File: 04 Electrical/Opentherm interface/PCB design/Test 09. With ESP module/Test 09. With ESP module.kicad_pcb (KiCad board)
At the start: 2 copper layers, 72 x 32 mm, 31 parts, among them J1 OpenTherm, J2 Laser range sensor, J3 ST7789, J4 Encoder, J6 USB_C_Receptacle_USB2.0_16P, Q1 MMBT2907A, U1 DS18S20, U2 DS18S20, U3 DS18S20, U4 DS18S20, U5 EL357N-G, U6 EL357N-G, U7 mini_esp32, U8 ESP32-S3-WROOM-1

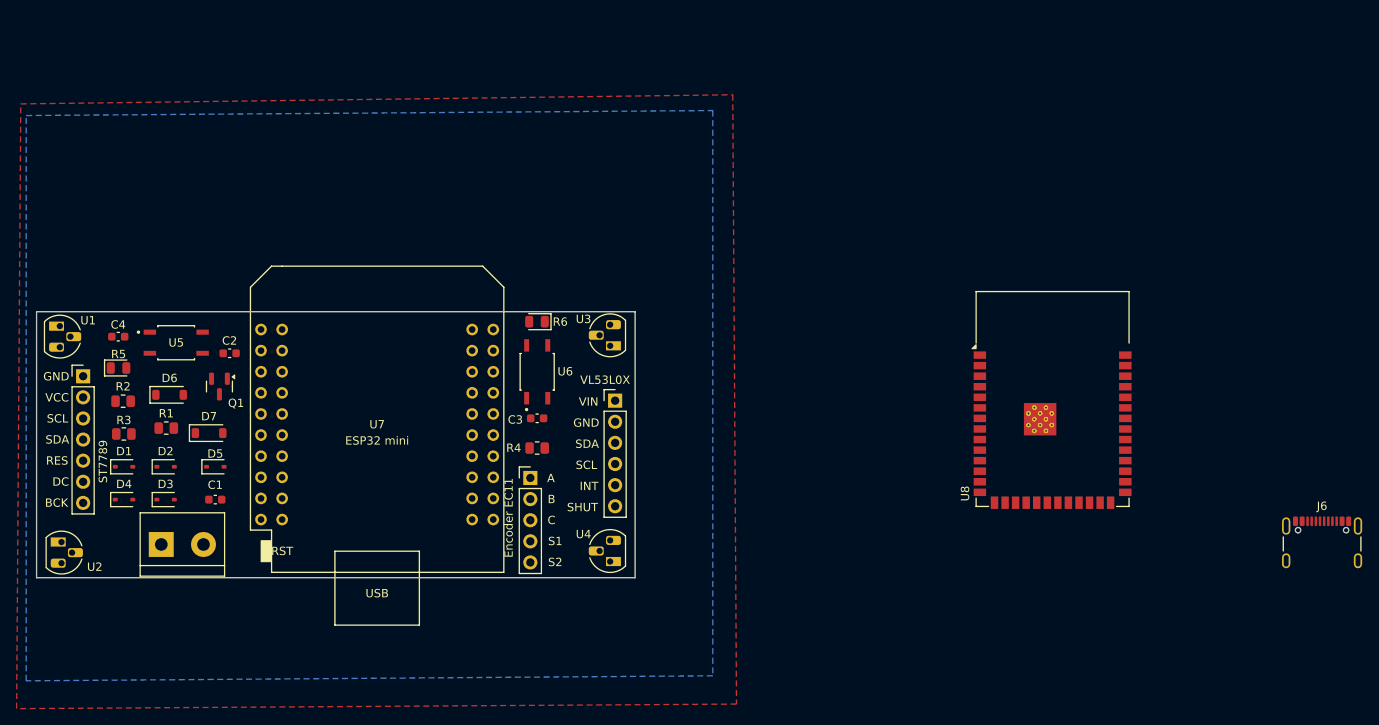
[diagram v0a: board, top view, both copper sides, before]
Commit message: First version of PCB without errors
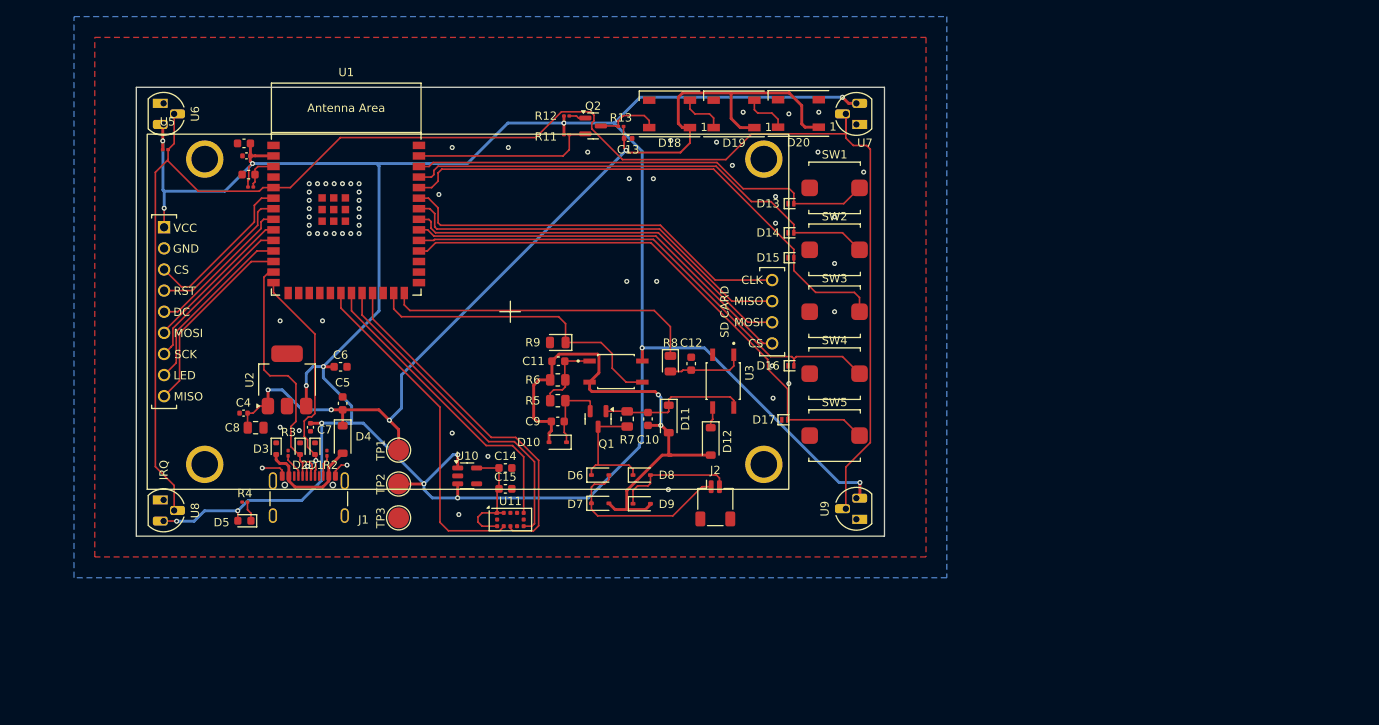
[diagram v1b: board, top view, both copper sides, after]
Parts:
- removed J3: ST7789, Connector_PinHeader_2.54mm:PinHeader_1x07_P2.54mm_Vertical
- removed J4: Encoder, Connector_PinHeader_2.54mm:PinHeader_1x05_P2.54mm_Vertical
- removed J6: USB_C_Receptacle_USB2.0_16P, Connector_USB:USB_C_Receptacle_GCT_USB4105-xx-A_16P_TopMnt_Horizontal
- added C10: 2n2, Capacitor_SMD:C_0603_1608Metric, F.Cu at (166.6, 87.9)
- added C11: 10n, Capacitor_SMD:C_0603_1608Metric, F.Cu at (155.8, 81.0)
- added C12: 2n2, Capacitor_SMD:C_0603_1608Metric, F.Cu at (171.8, 81.2)
- added C13: 10u, Capacitor_SMD:C_0402_1005Metric, F.Cu at (164.2, 54.1)
- added C14: 0.1u, Capacitor_SMD:C_0603_1608Metric, F.Cu at (149.4, 93.8)
- added C15: 4.7pF, Capacitor_SMD:C_0603_1608Metric, F.Cu at (149.4, 96.3)
- added C5: 0.1u, Capacitor_SMD:C_0603_1608Metric, F.Cu at (129.8, 86.0)
- added C6: 0.1u, Capacitor_SMD:C_0603_1608Metric, F.Cu at (129.6, 81.6)
- added C7: 10u, Capacitor_SMD:C_0402_1005Metric, F.Cu at (126.0, 88.9)
- added C8: 22u, Capacitor_SMD:C_0805_2012Metric, F.Cu at (119.3, 89.0)
- added C9: 10n, Capacitor_SMD:C_0603_1608Metric, F.Cu at (155.7, 88.2)
- added D10: BZT52C4V7S, Diode_SMD:D_SOD-323, F.Cu at (155.7, 90.7)
- added D11: BZT52C15V, Diode_SMD:D_SOD-123, F.Cu at (169.1, 87.9)
- added D12: BZT52C4V3, Diode_SMD:D_SOD-123, F.Cu at (174.1, 90.6)
- added D13: LESD8D3.3CAT5G-ES, Diode_SMD:D_SOD-882, F.Cu at (183.8, 62.0)
- added D14: LESD8D3.3CAT5G-ES, Diode_SMD:D_SOD-882, F.Cu at (183.8, 65.5)
- added D15: LESD8D3.3CAT5G-ES, Diode_SMD:D_SOD-882, F.Cu at (183.8, 68.5)
- added D16: LESD8D3.3CAT5G-ES, Diode_SMD:D_SOD-882, F.Cu at (183.8, 81.5)
- added D17: LESD8D3.3CAT5G-ES, Diode_SMD:D_SOD-882, F.Cu at (183.0, 88.0)
- added D18: WS2812B-2020, LED_SMD:LED_WS2812B_PLCC4_5.0x5.0mm_P3.2mm, F.Cu at (169.2, 51.2)
- added D19: WS2812B-2020, LED_SMD:LED_WS2812B_PLCC4_5.0x5.0mm_P3.2mm, F.Cu at (176.9, 51.2)
- added D20: WS2812B-2020, LED_SMD:LED_WS2812B_PLCC4_5.0x5.0mm_P3.2mm, F.Cu at (184.7, 51.1)
- added D8: 1N4148WS, Diode_SMD:D_SOD-323, F.Cu at (165.8, 94.7)
- added D9: 1N4148WS, Diode_SMD:D_SOD-323, F.Cu at (165.8, 98.1)
- added Q2: LBSS138LT1G-ES, Package_TO_SOT_SMD:SOT-23, F.Cu at (159.9, 52.6)
- added R10: 4k7, Resistor_SMD:R_0201_0603Metric, F.Cu at (108.5, 55.5)
- added R11: 10k, Resistor_SMD:R_0201_0603Metric, F.Cu at (156.8, 53.7)
- added R12: 10k, Resistor_SMD:R_0201_0603Metric, F.Cu at (156.8, 51.5)
- added R13: 10k, Resistor_SMD:R_0201_0603Metric, F.Cu at (163.3, 52.7)
- added R7: 330, Resistor_SMD:R_0805_2012Metric, F.Cu at (164.1, 87.9)
- added R8: 1k5, Diode_SMD:D_0805_2012Metric, F.Cu at (169.2, 81.2)
- added R9: 330, Diode_SMD:D_0805_2012Metric, F.Cu at (155.7, 78.7)
- added SW1: btn_home, Project:SW_Push_SPEH, F.Cu at (189.0, 60.1)
- added SW2: btn_up, Project:SW_Push_SPEH, F.Cu at (189.0, 67.5)
- added SW3: btn_down, Project:SW_Push_SPEH, F.Cu at (189.0, 75.0)
- added SW4: btn_confirm, Project:SW_Push_SPEH, F.Cu at (189.0, 82.5)
- added SW5: btn_back, Project:SW_Push_SPEH, F.Cu at (189.0, 89.9)
- added TP1: 5V, TestPoint:TestPoint_Pad_D2.5mm, F.Cu at (136.6, 91.7)
- added TP2: 3V3, TestPoint:TestPoint_Pad_D2.5mm, F.Cu at (136.6, 95.7)
- added TP3: GND, TestPoint:TestPoint_Pad_D2.5mm, F.Cu at (136.6, 99.8)
- added U10: LP5907MFX-2.8/NOPB, Package_TO_SOT_SMD:SOT-23-5, F.Cu at (144.8, 94.8)
- added U11: VL53L0CXV0DH/1, Sensor_Distance:ST_VL53L1x, F.Cu at (150.0, 100.0)
- added U9: DS18S20, Package_TO_SOT_THT:TO-92L_HandSolder, F.Cu at (191.6, 100.0)
- C1: value 10n -> 1u
- C2: value 2n2 -> 0.1u
- C3: value 10n -> 10u; footprint Capacitor_SMD:C_0603_1608Metric -> Capacitor_SMD:C_0402_1005Metric
- C4: value 2n2 -> 10u; footprint Capacitor_SMD:C_0603_1608Metric -> Capacitor_SMD:C_0402_1005Metric
- D1, D2, D3: value 1N4148WS -> LESD5D5.0CT1G; footprint Diode_SMD:D_SOD-323 -> Diode_SMD:D_SOD-523
- D4: value 1N4148WS -> 1N5819HW-7-F; footprint Diode_SMD:D_SOD-323 -> Diode_SMD:D_SOD-123
- D5: value BZT52C4V7S -> C2286; footprint Diode_SMD:D_SOD-323 -> LED_SMD:LED_0603_1608Metric
- D6: value BZT52C15V -> 1N4148WS; footprint Diode_SMD:D_SOD-123 -> Diode_SMD:D_SOD-323
- D7: value BZT52C4V3 -> 1N4148WS; footprint Diode_SMD:D_SOD-123 -> Diode_SMD:D_SOD-323
- J1: value OpenTherm -> USB-C port; footprint TerminalBlock:TerminalBlock_bornier-2_P5.08mm -> Connector_USB:USB_C_Receptacle_GCT_USB4105-xx-A_16P_TopMnt_Horizontal
- J2: value Laser range sensor -> Boiler; footprint Connector_PinHeader_2.54mm:PinHeader_1x06_P2.54mm_Vertical -> Connector_JST:JST_SH_SM02B-SRSS-TB_1x02-1MP_P1.00mm_Horizontal
- R1: value 200 -> 10k; footprint Resistor_SMD:R_0805_2012Metric -> Resistor_SMD:R_0201_0603Metric
- R2: value 150 -> 4k7; footprint Resistor_SMD:R_0805_2012Metric -> Resistor_SMD:R_0201_0603Metric
- R3: value 330 -> 4k7; footprint Resistor_SMD:R_0805_2012Metric -> Resistor_SMD:R_0201_0603Metric
- R4: value 4k7 -> 5k1; footprint Resistor_SMD:R_0805_2012Metric -> Resistor_SMD:R_0201_0603Metric
- R5: value 1k5 -> 200; footprint Diode_SMD:D_0805_2012Metric -> Resistor_SMD:R_0805_2012Metric
- R6: value 330 -> 150; footprint Diode_SMD:D_0805_2012Metric -> Resistor_SMD:R_0805_2012Metric
- U1: value DS18S20 -> ESP32-S3-WROOM-1-N8R2; footprint Package_TO_SOT_THT:TO-92L_HandSolder -> PCM_Espressif:ESP32-S3-WROOM-1
- U2: value DS18S20 -> SGM2212-3.3XKC3G/TR; footprint Package_TO_SOT_THT:TO-92L_HandSolder -> Package_TO_SOT_SMD:SOT-223-3_TabPin2
- U3, U4: value DS18S20 -> EL357N-G; footprint Package_TO_SOT_THT:TO-92L_HandSolder -> EL357N-G:OPTO_EL357N-G
- U5: value EL357N-G -> ILI9341_no_touch; footprint EL357N-G:OPTO_EL357N-G -> Project:ILI9341_no_touch
- U6: value EL357N-G -> DS18S20; footprint EL357N-G:OPTO_EL357N-G -> Package_TO_SOT_THT:TO-92L_HandSolder
- U7: value mini_esp32 -> DS18S20; footprint ESP32_mini:ESP32_mini -> Package_TO_SOT_THT:TO-92L_HandSolder
- U8: value ESP32-S3-WROOM-1 -> DS18S20; footprint RF_Module:ESP32-S3-WROOM-1 -> Package_TO_SOT_THT:TO-92L_HandSolder
- moved U8 107.6 mm to (108.3, 97.6), turned to -90 degrees
- moved U7 68.0 mm to (191.6, 52.5), turned to 90 degrees
- moved U6 55.3 mm to (108.3, 49.9), turned to -90 degrees
- moved R5 53.0 mm to (155.7, 85.7), turned to 180 degrees
- moved D6 52.7 mm to (160.8, 94.7)
- moved D7 47.8 mm to (160.8, 98.0)
- moved C3 47.1 mm to (118.2, 56.2)
- moved Q1 45.7 mm to (160.6, 87.9)
- moved U5 40.4 mm to (150.0, 75.0)
- moved C1 39.3 mm to (118.5, 58.5)
- moved U1 37.0 mm to (130.2, 63.2), turned to 0 degrees
- moved R4 35.8 mm to (118.0, 97.9)
- moved U2 33.4 mm to (123.1, 83.2), turned to 90 degrees
- moved R1 30.7 mm to (118.8, 60.0)
- moved D4 27.3 mm to (129.8, 90.4), turned to -90 degrees
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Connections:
- C1 pad 1: GND -> Net-(U1-EN)
- C1 pad 2: Net-(D5-K) -> GND
- C2 pad 1: Net-(D6-K) -> VCC_3V3
- C3 pad 1: GND -> VCC_3V3
- C3 pad 2: Net-(C3-Pad2) -> GND
- C4 pad 1: GND -> VCC_5V
- C4 pad 2: Net-(C4-Pad2) -> GND
- D1 pad 1: Net-(D1-K) -> GND
- D1 pad 2: Net-(D1-A) -> USB D+
- D2 pad 1: Net-(D1-A) -> GND
- D2 pad 2: GND -> USB D-
- D3 pad 1: Net-(D1-K) -> GND
- D3 pad 2: Net-(D3-A) -> Vusb
- D4 pad 1: Net-(D3-A) -> VCC_5V
- D4 pad 2: GND -> Vusb
- D5 pad 2: GND -> VCC_3V3
- D6 pad 2: GND -> Net-(D6-A)
- D7 pad 1: Net-(D7-K) -> Net-(D6-A)
- D7 pad 2: GND -> GND1
- J2 pad 1: +3V3 -> Net-(D6-A)
- J2 pad 2: GND -> Net-(D8-A)
- Q1 pad 1: Net-(D6-K) -> Net-(D11-K)
- Q1 pad 2: Net-(D5-K) -> Net-(D10-K)
- Q1 pad 3: Net-(D1-K) -> Net-(D6-K)
- R1 pad 1: Net-(D5-K) -> Net-(U1-EN)
- R1 pad 2: Net-(C3-Pad2) -> VCC_3V3
- R2 pad 1: Net-(C3-Pad2) -> GND
- R2 pad 2: GND -> Net-(J1-CC2)
- R3 pad 1: Net-(D6-K) -> GND
- R3 pad 2: Net-(D1-K) -> Net-(J1-CC1)
- R4 pad 1: +3V3 -> GND
- R4 pad 2: onewire -> Net-(D5-K)
- R5 pad 1: boil_to_cntr -> Net-(D10-K)
- R5 pad 2: Net-(C4-Pad2) -> Net-(C11-Pad2)
- R6 pad 1: cntr_to_boil -> Net-(C11-Pad2)
- R6 pad 2: GND -> GND1
- U1 pad 2: onewire -> VCC_3V3
- U1 pad 3: +3V3 -> Net-(U1-EN)
- U2 pad 1: GND -> VCC_5V
- U2 pad 2: onewire -> GND
- U2 pad 3: +3V3 -> VCC_3V3
- U3 pad 1: GND -> Net-(C12-Pad2)
- U3 pad 2: onewire -> GND
- U3 pad 3: +3V3 -> Net-(D12-K)
- U4 pad 1: GND -> Net-(C11-Pad2)
- U4 pad 2: onewire -> GND1
- U4 pad 3: +3V3 -> cntr_to_boil
- U5 pad 1: Net-(C4-Pad2) -> VCC_3V3
- U5 pad 3: Net-(D7-K) -> Disp_CS
- U5 pad 4: Net-(D6-K) -> Disp_RES
- U6 pad 1: Net-(C3-Pad2) -> GND
- U6 pad 2: GND -> onewire
- U6 pad 3: cntr_to_boil -> VCC_3V3
- U7 pad 2: GND -> onewire
- U7 pad 3: unconnected-(U7-NC-Pad3) -> VCC_3V3
- U8 pad 2: unconnected-(U8-3V3-Pad2) -> onewire
- U8 pad 3: unconnected-(U8-EN-Pad3) -> VCC_3V3
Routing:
- net VCC_3V3: track 0.00 -> 327.3 mm, vias 0 -> 15
- net onewire: track 0.00 -> 195.0 mm
- net VCC_5V: track 0.00 -> 119.4 mm, vias 0 -> 4
- net btn_back: track 0.00 -> 65.9 mm
- net btn_down: track 0.00 -> 64.1 mm
- net GND1: track 0.00 -> 62.1 mm, vias 0 -> 2
- net btn_confirm: track 0.00 -> 61.6 mm
- net btn_up: track 0.00 -> 58.6 mm
- net btn_home: track 0.00 -> 56.8 mm
- net SD_CS: track 0.00 -> 48.1 mm
- net SD_MOSI: track 0.00 -> 48.1 mm
- net SD_MISO: track 0.00 -> 48.0 mm
- net SD_SCK: track 0.00 -> 47.6 mm
- net TOF_SDA: track 0.00 -> 42.1 mm
- net TOF_SCL: track 0.00 -> 40.9 mm
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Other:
- board size 72 x 32 mm -> 90 x 54 mm
- board text removed: "A"
- board text removed: "B"
- board text removed: "BCK"
- board text removed: "C"
- board text removed: "DC"
- board text removed: "ESP32 mini"
- board text removed: "Encoder EC11"
- board text removed: "GND"
- board text removed: "INT"
- board text removed: "RES"
- board text removed: "S1"
- board text removed: "S2"
- board text removed: "SCL"
- board text removed: "SDA"
- board text removed: "SHUT"
- board text removed: "ST7789"
- board text removed: "VCC"
- board text removed: "VIN"
- board text removed: "VL53L0X"

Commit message: Schematic update
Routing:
- net Disp_MISO: track 23.2 -> 27.2 mm
- net Disp_LED: track 21.5 -> 25.2 mm
- net Disp_SCK: track 20.0 -> 23.4 mm
- net Disp_MOSI: track 18.4 -> 21.5 mm
- net Disp_CS: track 19.6 -> 16.7 mm
- net Disp_DC: track 18.2 -> 19.5 mm
- net Disp_RES: track 18.2 -> 17.6 mm
- net GND: vias 58 -> 86
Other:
- board text added: "3V3"
- board text added: "5V"
- board text added: "BACK"
- board text added: "CONFIRM"
- board text added: "DOWN"
- board text added: "GND"
- board text added: "HOME"
- board text added: "UP"

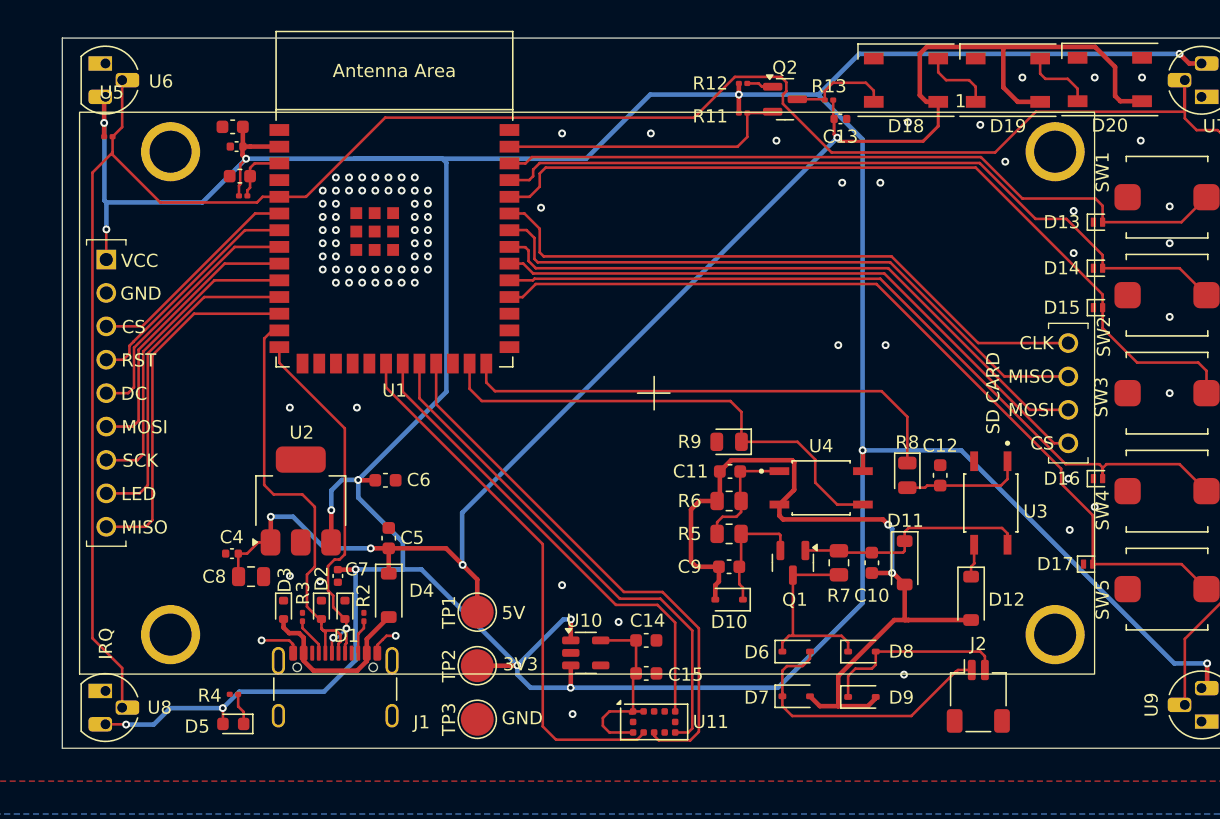
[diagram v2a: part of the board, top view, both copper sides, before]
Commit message: SPI port on default pins
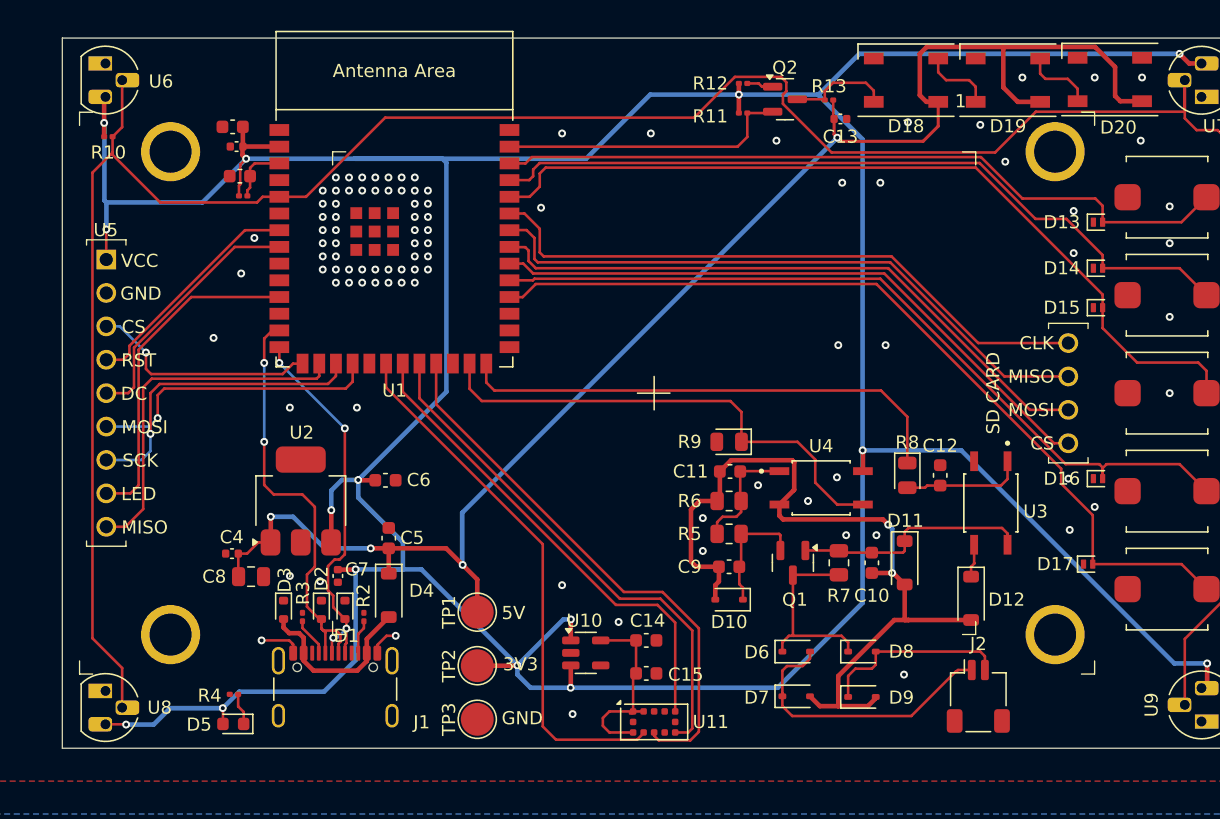
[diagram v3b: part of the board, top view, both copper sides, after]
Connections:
- U1 pad 10: Disp_SCK -> unconnected-(U1-GPIO17/U1TXD/ADC2_CH6-Pad10)
- U1 pad 12: Disp_MISO -> unconnected-(U1-GPIO8/TOUCH8/ADC1_CH7/SUBSPICS1-Pad12)
- U1 pad 15: unconnected-(U1-GPIO3/TOUCH3/ADC1_CH2-Pad15) -> Disp_CS
- U1 pad 16: unconnected-(U1-GPIO46-Pad16) -> Disp_MISO
- U1 pad 17: unconnected-(U1-GPIO9/TOUCH9/ADC1_CH8/FSPIHD/SUBSPIHD-Pad17) -> Disp_SCK
- U1 pad 18: unconnected-(U1-GPIO10/TOUCH10/ADC1_CH9/FSPICS0/FSPIIO4/SUBSPICS0-Pad18) -> Disp_MOSI
- U1 pad 6: Disp_CS -> unconnected-(U1-GPIO6/TOUCH6/ADC1_CH5-Pad6)
- U1 pad 9: Disp_MOSI -> unconnected-(U1-GPIO16/U0CTS/ADC2_CH5/XTAL_32K_N-Pad9)
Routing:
- net Disp_MOSI: track 21.5 -> 22.5 mm, vias 0 -> 1
- net Disp_CS: track 16.7 -> 17.5 mm, vias 0 -> 1
- net Disp_SCK: track 23.4 -> 23.6 mm, vias 0 -> 1
- net USB D-: vias 0 -> 2
- net USB D+: vias 2 -> 4
- net GND: vias 86 -> 96

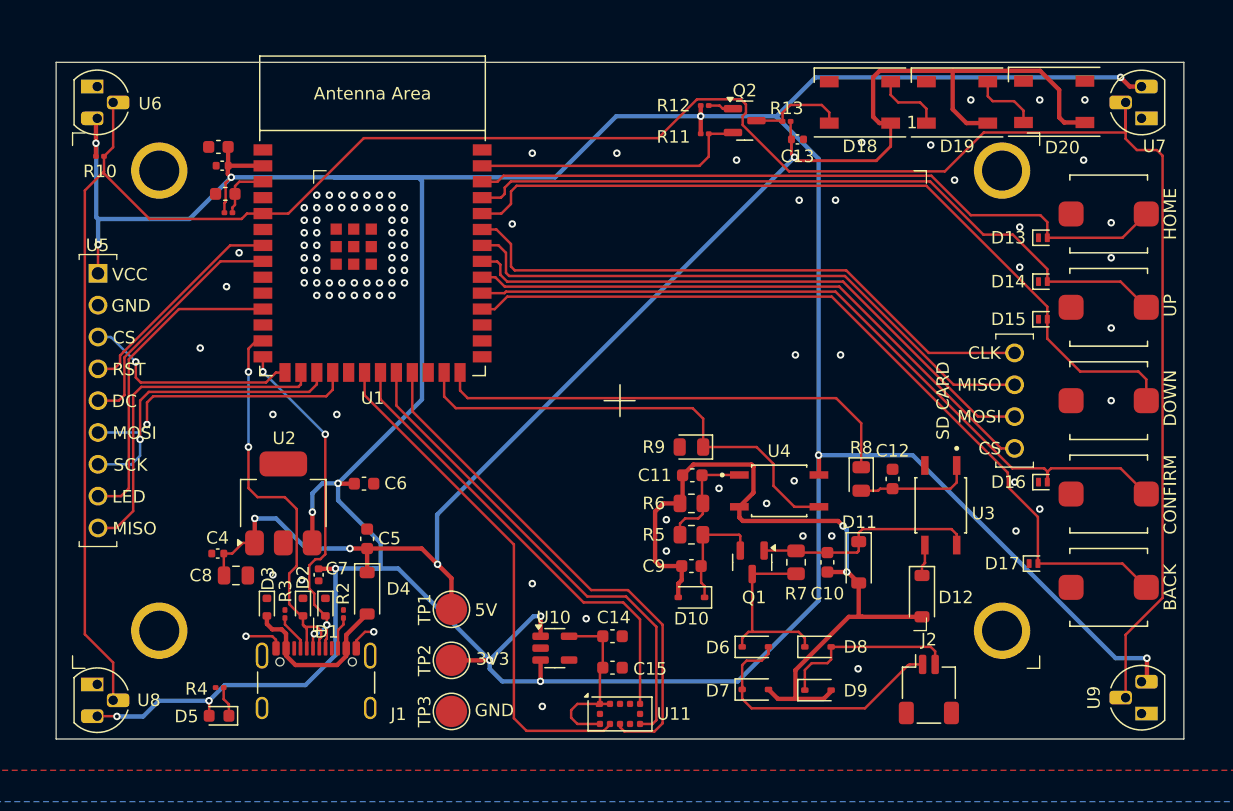
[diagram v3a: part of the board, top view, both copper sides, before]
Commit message: Component assignment
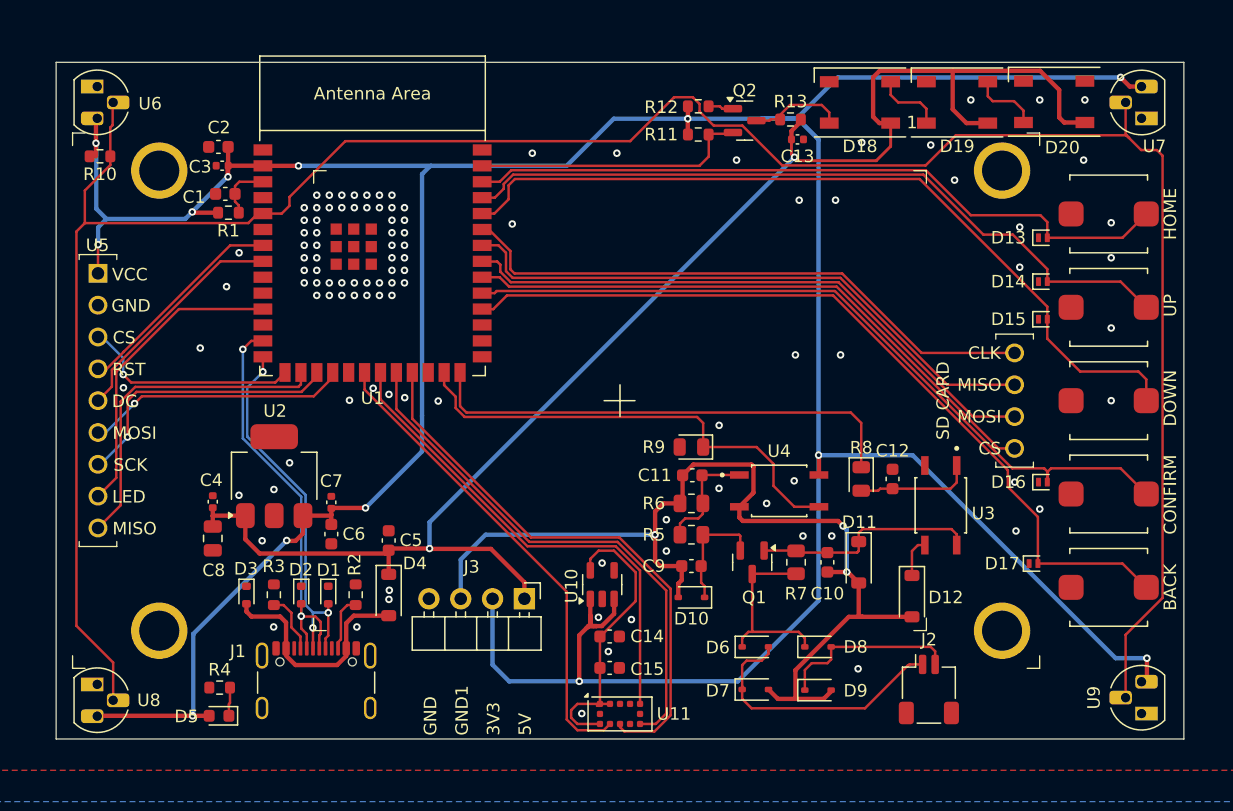
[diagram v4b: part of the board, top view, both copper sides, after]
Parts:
- removed TP1: 5V, TestPoint:TestPoint_Pad_D2.5mm
- removed TP2: 3V3, TestPoint:TestPoint_Pad_D2.5mm
- removed TP3: GND, TestPoint:TestPoint_Pad_D2.5mm
- added J3: Test connector, Project:PinHeader_1x04_P2.54mm_Horizontal, F.Cu at (142.4, 90.8)
- D5: value C2286 -> XL-1608UGC-04
- R1, R10, R11, R12, R13, R2, R3, R4: footprint Resistor_SMD:R_0201_0603Metric -> Resistor_SMD:R_0603_1608Metric
- moved U10 6.32 mm to (148.6, 89.7), turned to 90 degrees
- moved C7 5.87 mm to (127.0, 83.1), turned to 90 degrees
- moved C6 4.80 mm to (127.0, 85.7), turned to -90 degrees
- moved C4 4.15 mm to (117.5, 83.1), turned to 90 degrees
- moved C8 3.49 mm to (117.5, 86.0), turned to -90 degrees
- moved U2 2.29 mm to (122.4, 81.0)
- moved D3 1.89 mm to (120.2, 90.5)
- moved R2 1.82 mm to (128.9, 90.5)
- moved R3 1.77 mm to (122.4, 90.5)
- moved D4 1.73 mm to (131.5, 90.5)
- moved C5 1.73 mm to (131.5, 86.2)
- moved D1 0.99 mm to (126.7, 90.5)
- moved D2 0.97 mm to (124.6, 90.5)
- moved D12 0.80 mm to (173.3, 90.6)
- moved R11 0.52 mm to (156.2, 53.8)
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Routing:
- net VCC_3V3: track 327.3 -> 298.6 mm, vias 15 -> 13
- net GND1: track 62.1 -> 80.4 mm, vias 2 -> 3
- net Net-(U10-OUT): track 14.6 -> 23.4 mm
- net GND: track 5.50 -> 0.00 mm, vias 96 -> 107
- net Vusb: track 13.7 -> 17.9 mm
- net VCC_5V: track 119.5 -> 123.5 mm, vias 4 -> 2
- net TOF_GPIO01: track 39.6 -> 42.7 mm
- net onewire: track 195.0 -> 192.0 mm
- net TOF_SDA: track 42.1 -> 45.0 mm
- net TOF_SCL: track 40.9 -> 38.4 mm
- net TOF_XSHUT: track 36.9 -> 39.2 mm
- net Net-(J1-CC1): track 2.94 -> 4.79 mm
- net Net-(J1-CC2): track 2.60 -> 4.43 mm
- net USB D+: track 29.2 -> 30.8 mm, vias 4 -> 3
- net Disp_MOSI: track 22.5 -> 21.0 mm
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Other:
- board text added: "GND1"
